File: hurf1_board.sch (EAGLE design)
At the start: 32 parts, among them IC1 STM32F10XCXT6, J1 0R, J2 0R, X1 MINI-USB-32005-201, Y1 8MHz

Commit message: Schematic Completed -schematic w1 -board w1 -controlboard sketch added (.dxf) =.gitignore updated = hurf1_schematic.sch -> hurf1_board.sch = board images added
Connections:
- net SPI1_SS renamed SPI1_NSS
- net USB_N renamed USB_DM
- net USB_P renamed USB_DP
- net ESC1: now also IC1PORTB_L.PB0
- net ESC2: now also IC1PORTB_L.PB1
- net ESC3: now also IC1PORTB_H.PB10
- net ESC4: now also IC1PORTB_H.PB11
- net MPU_INT: now also IC1PORTA_L.PA3
- net RC_IN1: now also IC1PORTB_H.PB9
- net RC_IN2: now also IC1PORTB_H.PB8
- net RC_IN3: now also IC1PORTB_L.PB7
- net RC_IN4: now also IC1PORTB_L.PB6
- net RC_IN5: now also IC1PORTB_L.PB3
- net RC_IN6: now also IC1PORTA_H.PA15
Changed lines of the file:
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@@
 <setting verticaltext="up"/>
 </settings>
-<grid distance="0.1" unitdist="inch" unit="inch" style="lines" multiple="1" display="yes" altdistance="0.01" altunitdist="inch" altunit="inch"/>
+<grid distance="0.1" unitdist="inch" unit="inch" style="lines" multiple="1" display="no" altdistance="0.01" altunitdist="inch" altunit="inch"/>
 <layers>
 <layer number="1" name="Top" color="4" fill="1" visible="no" active="no"/>
@@
 <wire x1="76.2" y1="63.5" x2="73.66" y2="63.5" width="0.1524" layer="91"/>
 <junction x="73.66" y="63.5"/>
-<wire x1="73.66" y1="63.5" x2="71.12" y2="63.5" width="0.1524" layer="91"/>
-<label x="71.12" y="63.5" size="1.778" layer="95" rot="R180" xref="yes"/>
+<wire x1="73.66" y1="63.5" x2="72.644" y2="63.5" width="0.1524" layer="91"/>
+<label x="72.644" y="63.5" size="1.778" layer="95" rot="R180" xref="yes"/>
 </segment>
 <segment>
@@
 </segment>
 </net>
-<net name="SPI1_SS" class="0">
+<net name="SPI1_NSS" class="0">
 <segment>
 <pinref part="IC1" gate="PORTA_L" pin="PA4"/>
@@
 </segment>
 </net>
-<net name="USB_N" class="0">
+<net name="USB_DM" class="0">
 <segment>
 <pinref part="IC1" gate="PORTA_H" pin="PA11"/>
@@
 <wire x1="5.08" y1="30.48" x2="-5.08" y2="30.48" width="0.1524" layer="91"/>
 <label x="-5.08" y="30.48" size="1.778" layer="95" rot="R180" xref="yes"/>
-</segment>
-</net>
-<net name="USB_P" class="0">
-<segment>
-<pinref part="IC1" gate="PORTA_H" pin="PA12"/>
-<wire x1="5.08" y1="53.34" x2="2.54" y2="53.34" width="0.1524" layer="91"/>
-<label x="2.54" y="53.34" size="1.778" layer="95" rot="R180" xref="yes"/>
-</segment>
-<segment>
-<pinref part="R2" gate="G$1" pin="1"/>
-<label x="-5.08" y="25.4" size="1.778" layer="95" rot="R180" xref="yes"/>
-<wire x1="10.16" y1="25.4" x2="2.54" y2="25.4" width="0.1524" layer="91"/>
-<pinref part="R3" gate="G$1" pin="1"/>
-<wire x1="2.54" y1="25.4" x2="-5.08" y2="25.4" width="0.1524" layer="91"/>
-<wire x1="2.54" y1="17.78" x2="2.54" y2="25.4" width="0.1524" layer="91"/>
-<junction x="2.54" y="25.4"/>
 </segment>
 </net>
@@
 <wire x1="-2.54" y1="111.76" x2="-5.08" y2="111.76" width="0.1524" layer="91"/>
 <label x="-5.08" y="111.76" size="1.778" layer="95" rot="R180" xref="yes"/>
+</segment>
+<segment>
+<pinref part="IC1" gate="PORTA_L" pin="PA3"/>
+<wire x1="5.08" y1="81.28" x2="2.54" y2="83.82" width="0.1524" layer="91"/>
+<wire x1="2.54" y1="83.82" x2="2.032" y2="83.82" width="0.1524" layer="91"/>
+<label x="2.032" y="83.82" size="1.778" layer="95" rot="R180" xref="yes"/>
 </segment>
 </net>
@@
 <label x="109.22" y="124.46" size="1.778" layer="95" xref="yes"/>
 </segment>
+<segment>
+<pinref part="IC1" gate="PORTB_H" pin="PB9"/>
+<wire x1="38.1" y1="60.96" x2="51.562" y2="60.96" width="0.1524" layer="91"/>
+<label x="51.562" y="60.96" size="1.778" layer="95" xref="yes"/>
+</segment>
 </net>
 <net name="RC_IN2" class="0">
@@
 <wire x1="96.52" y1="129.54" x2="109.22" y2="129.54" width="0.1524" layer="91"/>
 <label x="109.22" y="129.54" size="1.778" layer="95" xref="yes"/>
+</segment>
+<segment>
+<pinref part="IC1" gate="PORTB_H" pin="PB8"/>
+<wire x1="38.1" y1="63.5" x2="40.64" y2="63.5" width="0.1524" layer="91"/>
+<label x="40.64" y="63.5" size="1.778" layer="95" xref="yes"/>
 </segment>
 </net>
@@
 <label x="109.22" y="134.62" size="1.778" layer="95" xref="yes"/>
 </segment>
+<segment>
+<pinref part="IC1" gate="PORTB_L" pin="PB7"/>
+<wire x1="38.1" y1="71.12" x2="53.34" y2="71.12" width="0.1524" layer="91"/>
+<label x="53.34" y="71.12" size="1.778" layer="95" xref="yes"/>
+</segment>
 </net>
 <net name="RC_IN4" class="0">
@@
 <label x="109.22" y="139.7" size="1.778" layer="95" xref="yes"/>
 </segment>
+<segment>
+<pinref part="IC1" gate="PORTB_L" pin="PB6"/>
+<wire x1="38.1" y1="73.66" x2="40.64" y2="73.66" width="0.1524" layer="91"/>
+<label x="40.64" y="73.66" size="1.778" layer="95" xref="yes"/>
+</segment>
 </net>
 <net name="RC_IN5" class="0">
@@
 <label x="109.22" y="144.78" size="1.778" layer="95" xref="yes"/>
 </segment>
+<segment>
+<pinref part="IC1" gate="PORTB_L" pin="PB3"/>
+<wire x1="38.1" y1="81.28" x2="40.64" y2="81.28" width="0.1524" layer="91"/>
+<label x="40.64" y="81.28" size="1.778" layer="95" xref="yes"/>
+</segment>
 </net>
 <net name="RC_IN6" class="0">
@@
 <label x="109.22" y="149.86" size="1.778" layer="95" xref="yes"/>
 </segment>
+<segment>
+<pinref part="IC1" gate="PORTA_H" pin="PA15"/>
+<wire x1="5.08" y1="45.72" x2="-10.16" y2="45.72" width="0.1524" layer="91"/>
+<label x="-10.16" y="45.72" size="1.778" layer="95" rot="R180" xref="yes"/>
+</segment>
 </net>
 <net name="ESC1" class="0">
@@
 <label x="-30.48" y="93.98" size="1.778" layer="95" xref="yes"/>
 </segment>
+<segment>
+<pinref part="IC1" gate="PORTB_L" pin="PB0"/>
+<wire x1="38.1" y1="88.9" x2="40.64" y2="88.9" width="0.1524" layer="91"/>
+<label x="40.64" y="88.9" size="1.778" layer="95" xref="yes"/>
+</segment>
 </net>
 <net name="ESC2" class="0">
@@
 <label x="-30.48" y="81.28" size="1.778" layer="95" xref="yes"/>
 </segment>
+<segment>
+<pinref part="IC1" gate="PORTB_L" pin="PB1"/>
+<wire x1="38.1" y1="86.36" x2="50.8" y2="86.36" width="0.1524" layer="91"/>
+<label x="50.8" y="86.36" size="1.778" layer="95" xref="yes"/>
+</segment>
 </net>
 <net name="ESC3" class="0">
@@
 <label x="-30.48" y="63.5" size="1.778" layer="95" xref="yes"/>
 </segment>
+<segment>
+<pinref part="IC1" gate="PORTB_H" pin="PB10"/>
+<wire x1="38.1" y1="58.42" x2="40.64" y2="58.42" width="0.1524" layer="91"/>
+<label x="40.64" y="58.42" size="1.778" layer="95" xref="yes"/>
+</segment>
 </net>
 <net name="ESC4" class="0">
@@
 <wire x1="-50.8" y1="50.8" x2="-30.48" y2="50.8" width="0.1524" layer="91"/>
 <label x="-30.48" y="50.8" size="1.778" layer="95" xref="yes"/>
+</segment>
+<segment>
+<pinref part="IC1" gate="PORTB_H" pin="PB11"/>
+<wire x1="38.1" y1="55.88" x2="50.8" y2="55.88" width="0.1524" layer="91"/>
+<label x="50.8" y="55.88" size="1.778" layer="95" xref="yes"/>
 </segment>
 </net>
@@
 </segment>
 </net>
+<net name="USB_DP" class="0">
+<segment>
+<pinref part="R2" gate="G$1" pin="1"/>
+<label x="-5.08" y="25.4" size="1.778" layer="95" rot="R180" xref="yes"/>
+<wire x1="10.16" y1="25.4" x2="2.54" y2="25.4" width="0.1524" layer="91"/>
+<pinref part="R3" gate="G$1" pin="1"/>
+<wire x1="2.54" y1="25.4" x2="-5.08" y2="25.4" width="0.1524" layer="91"/>
+<wire x1="2.54" y1="17.78" x2="2.54" y2="25.4" width="0.1524" layer="91"/>
+<junction x="2.54" y="25.4"/>
+</segment>
+<segment>
+<pinref part="IC1" gate="PORTA_H" pin="PA12"/>
+<wire x1="5.08" y1="53.34" x2="2.54" y2="53.34" width="0.1524" layer="91"/>
+<label x="2.54" y="53.34" size="1.778" layer="95" rot="R180" xref="yes"/>
+</segment>
+</net>

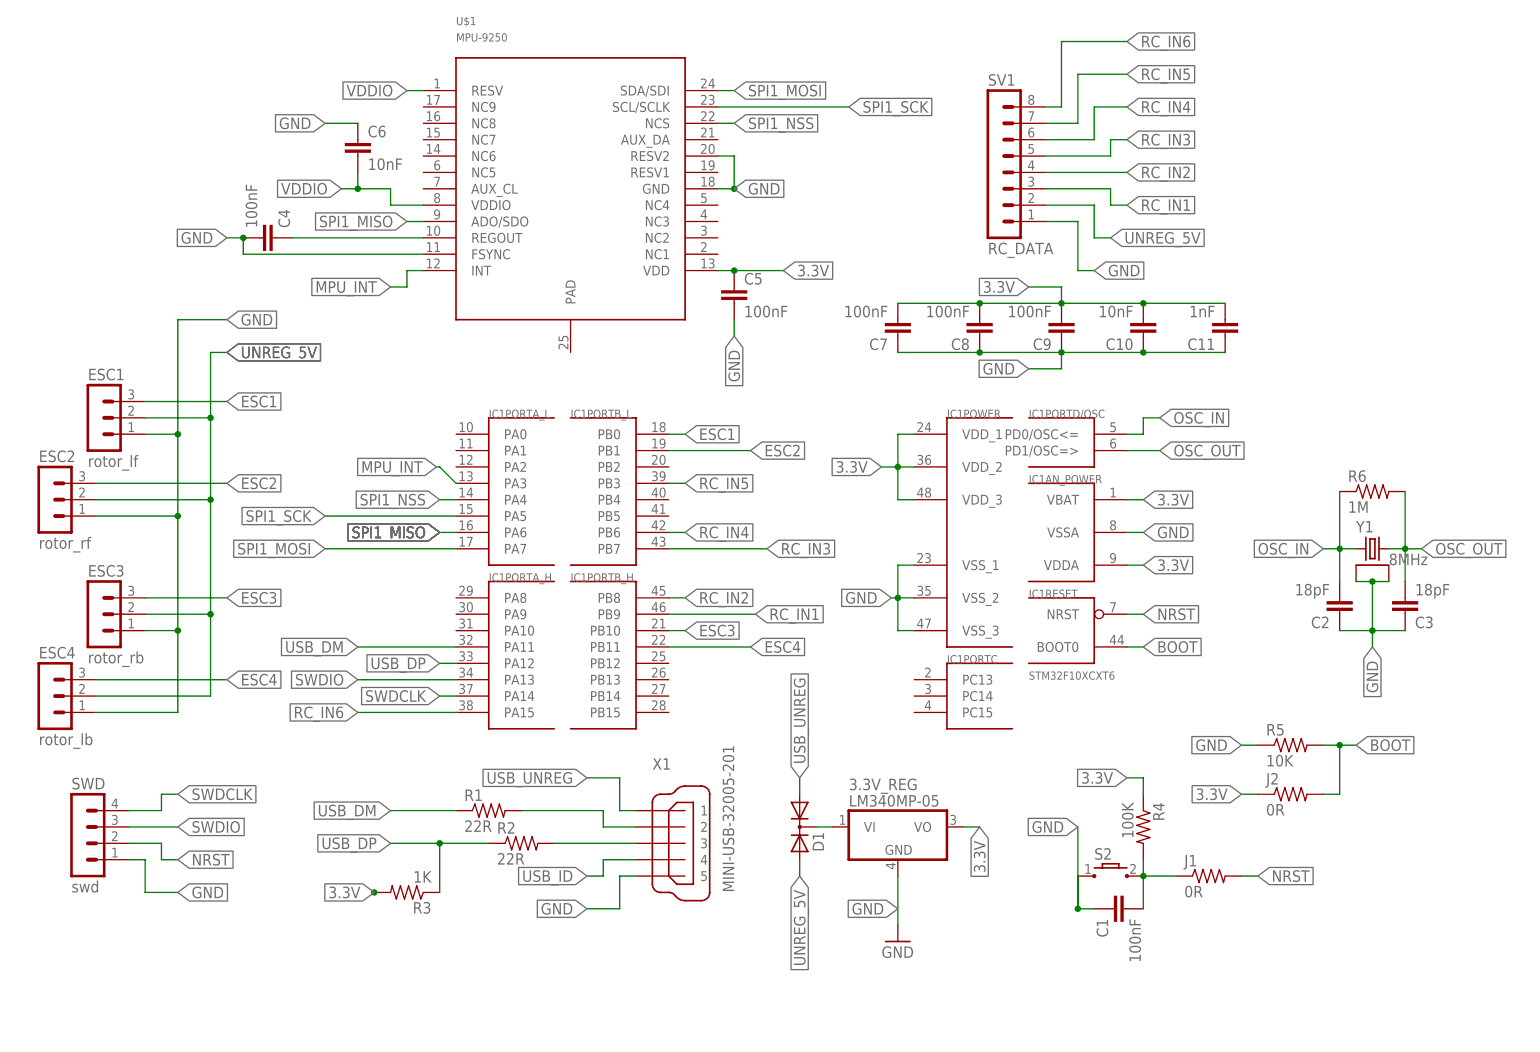
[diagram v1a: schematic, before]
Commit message: Circuit Size Shrinked -schematic w1 (updated) -board w1s1 (updated)  *SMD Package changed from 0805 -> 0603  *SWD Port changed from DIL -> JST-SH  X UNREG_5V pin must be connected to diode
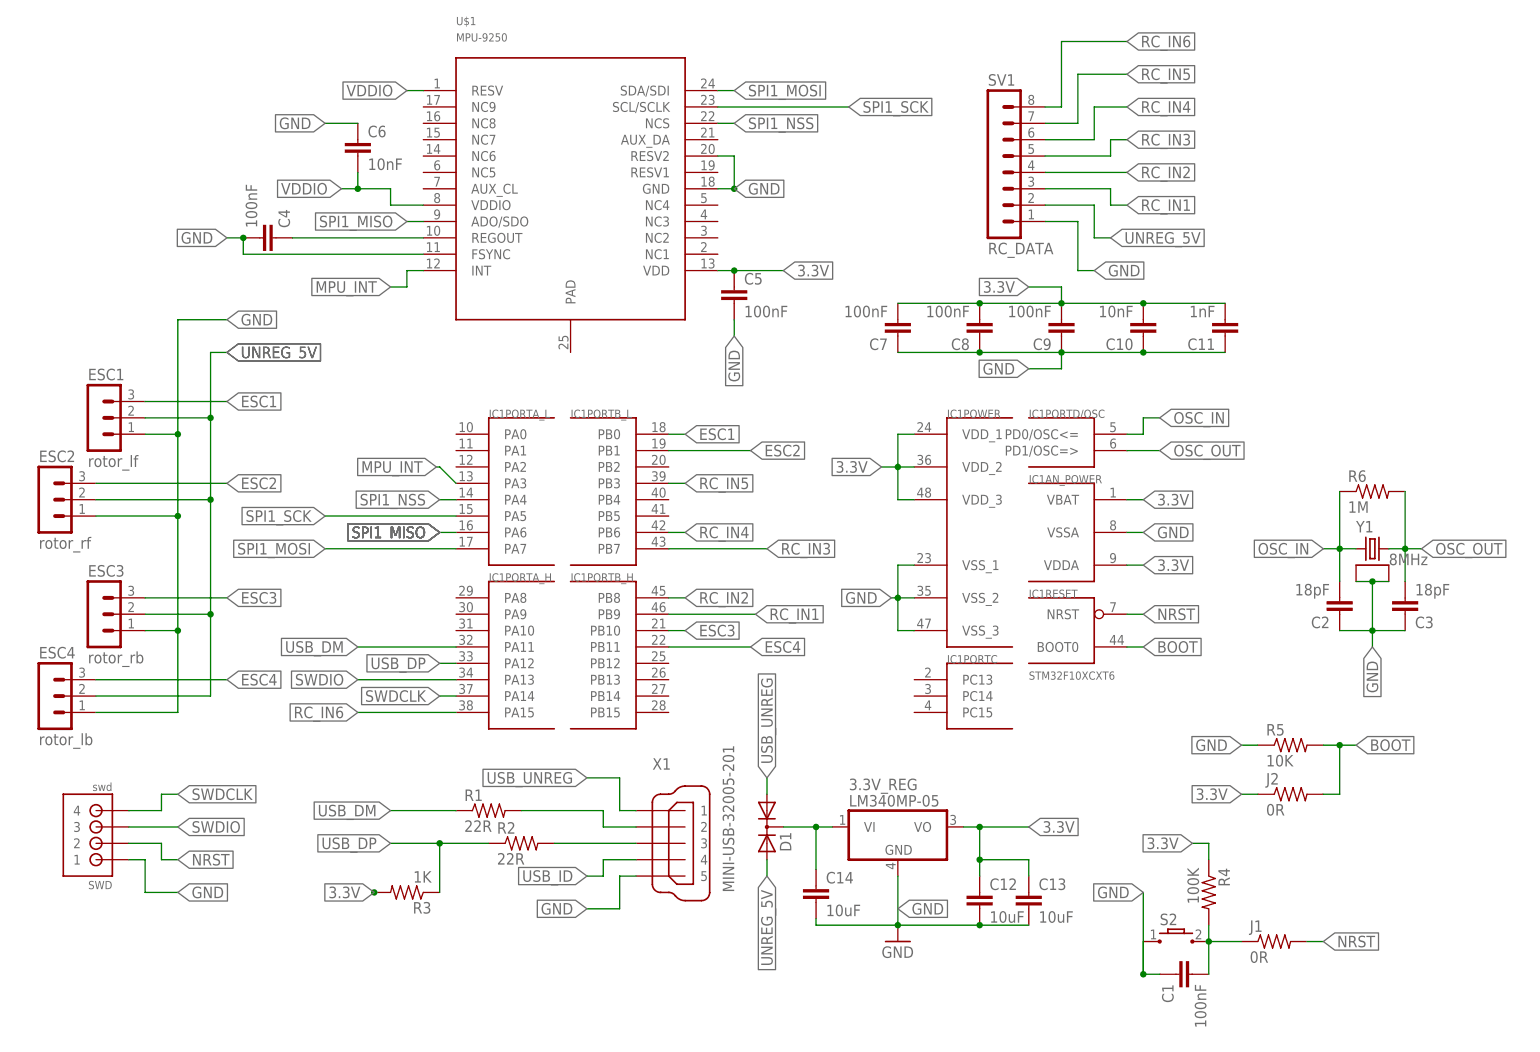
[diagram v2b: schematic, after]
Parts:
- added C12, C13, C14: 10uF, rcl:C-EUC0805
- C1, C10, C11, C2, C3, C5, C6, C7, C8, C9: device resistor:C-EUC0805K -> rcl:C-EUC0603
- J1, J2, R1, R2, R3, R4, R5, R6: device adafruit:R-US_M0805 -> rcl:R-US_R0603
- SWD: device con-lstb:MA04-1 -> SRG:JST-PH_4-PIN_HEADER
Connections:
- net 3.3V: now also C12.1, C13.1
- net GND: now also C12.2, C13.2, C14.2
- net N$4: now also C14.1
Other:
- moved on the sheet: C1, D1, J1, R4, S2

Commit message: Circuit Design Updated  -schematic w1(updated)   *1x Power Led , 2x Status Led Added   *RC_OUT and SWD packages updated  -board w1s1 (updated)   *All connections solved   *Schematic changes applied   X* RC_IN port MUST be updated from DIL -> JST-SH 8 Pin
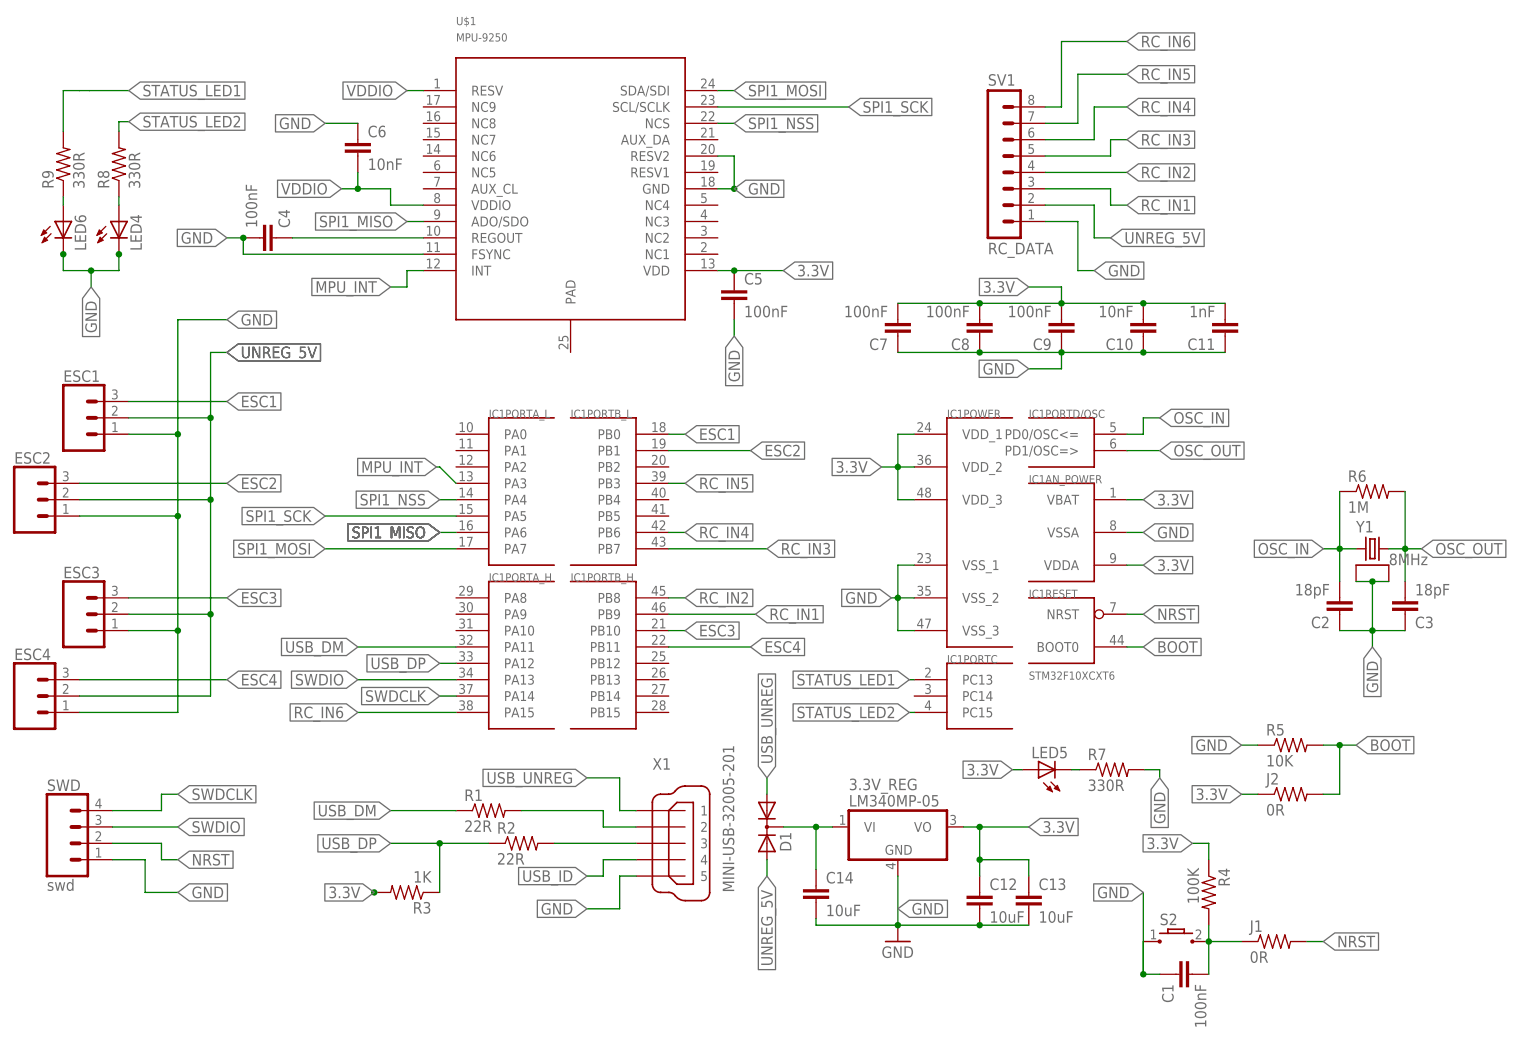
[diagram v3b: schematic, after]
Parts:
- added LED4, LED5, LED6: (no value), led:LEDSML0805
- added R7, R8, R9: 330R, rcl:R-US_R0603
- ESC1: value rotor_lf -> (none); device con-lstb:MA03-1 -> SparkFun-Connectors:CONN_03
- ESC2: value rotor_rf -> (none); device con-lstb:MA03-1 -> SparkFun-Connectors:CONN_03
- ESC3: value rotor_rb -> (none); device con-lstb:MA03-1 -> SparkFun-Connectors:CONN_03
- ESC4: value rotor_lb -> (none); device con-lstb:MA03-1 -> SparkFun-Connectors:CONN_03
- SWD: device SRG:JST-PH_4-PIN_HEADER -> SparkFun-Connectors:CONN_04SMD2
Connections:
- new net N$6: LED6.A, R9.1
- new net N$7: LED5.C, R7.1
- new net N$8: LED4.A, R8.1
- new net STATUS_LED1: IC1PORTC.PC13, R9.2
- new net STATUS_LED2: IC1PORTC.PC15, R8.2
- net 3.3V: now also LED5.A
- net GND: now also LED4.C, LED6.C, R7.2
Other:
- moved on the sheet: SWD
